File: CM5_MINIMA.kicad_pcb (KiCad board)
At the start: 4 copper layers, 54.6 x 57.1 mm, 97 parts, among them J101 USB_C_Receptacle_USB2.0, J501 690-019-298-412, J502 I2C, J601 JST_SHBM04B-SRSS-TB, Q501 DTC043ZEBTL, SW501 SW_Push, SW601 B3U-3000P, SW602 B3U-3000P, T401 7498111120AR, U401 TPD4EUSB30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

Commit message: production files added
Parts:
- added REF**: KiCad-Logo2_5mm_SilkScreen, Symbol:KiCad-Logo2_5mm_SilkScreen, F.Cu at (116.7, 77.8)

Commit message: JLCPCB
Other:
- board text added: "#808080FF"
- board text added: "0"
- board text added: "0 mm"
- board text added: "0.0000 mm / 0.0000 mm"
- board text added: "0.01 mm"
- board text added: "0.0152 mm"
- board text added: "0.02"
- board text added: "0.035 mm"
- board text added: "0.0994 mm"
- board text added: "0.3000 mm"
- board text added: "1"
- board text added: "1.265 mm"
- board text added: "1.5842 mm"
- board text added: "3.3"
- board text added: "4"
- board text added: "4.5"
- board text added: "54.5516 mm x 57.1400 mm"
- board text added: "B.Cu"
- board text added: "B.Mask"
- board text added: "B.Paste"
- board text added: "B.Silkscreen"
- board text added: "BOARD CHARACTERISTICS"
- board text added: "Board Thickness:"
- board text added: "Board overall dimensions:"
- board text added: "Bottom Silk Screen"
- board text added: "Bottom Solder Mask"
- board text added: "Bottom Solder Paste"
- board text added: "Castellated pads:"
- board text added: "Color"
- board text added: "Copper Finish:"
- board text added: "Copper Layer Count:"
- board text added: "Dielectric 1"
- board text added: "Dielectric 2"
- board text added: "Dielectric 3"
- board text added: "ENIG"
- board text added: "Edge card connectors:"
- board text added: "Epsilon R"
- board text added: "F.Cu"
- board text added: "F.Mask"
- board text added: "F.Paste"
- board text added: "F.Silkscreen"
- board text added: "FR4"
- board text added: "Impedance Control:"
- board text added: "In1.Cu"
- board text added: "In2.Cu"
- board text added: "Layer Name"
- board text added: "Loss Tangent"
- board text added: "Material"
- board text added: "Min hole diameter:"
- board text added: "Min track/spacing:"
- board text added: "No"
- board text added: "Not specified"
- board text added: "Plated Board Edge:"
- board text added: "Thickness (mm)"
- board text added: "Top Silk Screen"
- board text added: "Top Solder Mask"
- board text added: "Top Solder Paste"
- board text added: "Type"
- board text added: "Yes"
- board text added: "copper"
- board text added: "core"
- board text added: "prepreg"

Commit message: init
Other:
- board text removed: "#808080FF"
- board text removed: "0"
- board text removed: "0 mm"
- board text removed: "0.0000 mm / 0.0000 mm"
- board text removed: "0.01 mm"
- board text removed: "0.0152 mm"
- board text removed: "0.02"
- board text removed: "0.035 mm"
- board text removed: "0.0994 mm"
- board text removed: "0.3000 mm"
- board text removed: "1"
- board text removed: "1.265 mm"
- board text removed: "1.5842 mm"
- board text removed: "3.3"
- board text removed: "4"
- board text removed: "4.5"
- board text removed: "54.5516 mm x 57.1400 mm"
- board text removed: "B.Cu"
- board text removed: "B.Mask"
- board text removed: "B.Paste"
- board text removed: "B.Silkscreen"
- board text removed: "BOARD CHARACTERISTICS"
- board text removed: "Board Thickness:"
- board text removed: "Board overall dimensions:"
- board text removed: "Bottom Silk Screen"
- board text removed: "Bottom Solder Mask"
- board text removed: "Bottom Solder Paste"
- board text removed: "Castellated pads:"
- board text removed: "Color"
- board text removed: "Copper Finish:"
- board text removed: "Copper Layer Count:"
- board text removed: "Dielectric 1"
- board text removed: "Dielectric 2"
- board text removed: "Dielectric 3"
- board text removed: "ENIG"
- board text removed: "Edge card connectors:"
- board text removed: "Epsilon R"
- board text removed: "F.Cu"
- board text removed: "F.Mask"
- board text removed: "F.Paste"
- board text removed: "F.Silkscreen"
- board text removed: "FR4"
- board text removed: "Impedance Control:"
- board text removed: "In1.Cu"
- board text removed: "In2.Cu"
- board text removed: "Layer Name"
- board text removed: "Loss Tangent"
- board text removed: "Material"
- board text removed: "Min hole diameter:"
- board text removed: "Min track/spacing:"
- board text removed: "No"
- board text removed: "Not specified"
- board text removed: "Plated Board Edge:"
- board text removed: "Thickness (mm)"
- board text removed: "Top Silk Screen"
- board text removed: "Top Solder Mask"
- board text removed: "Top Solder Paste"
- board text removed: "Type"
- board text removed: "Yes"
- board text removed: "copper"
- board text removed: "core"
- board text removed: "prepreg"

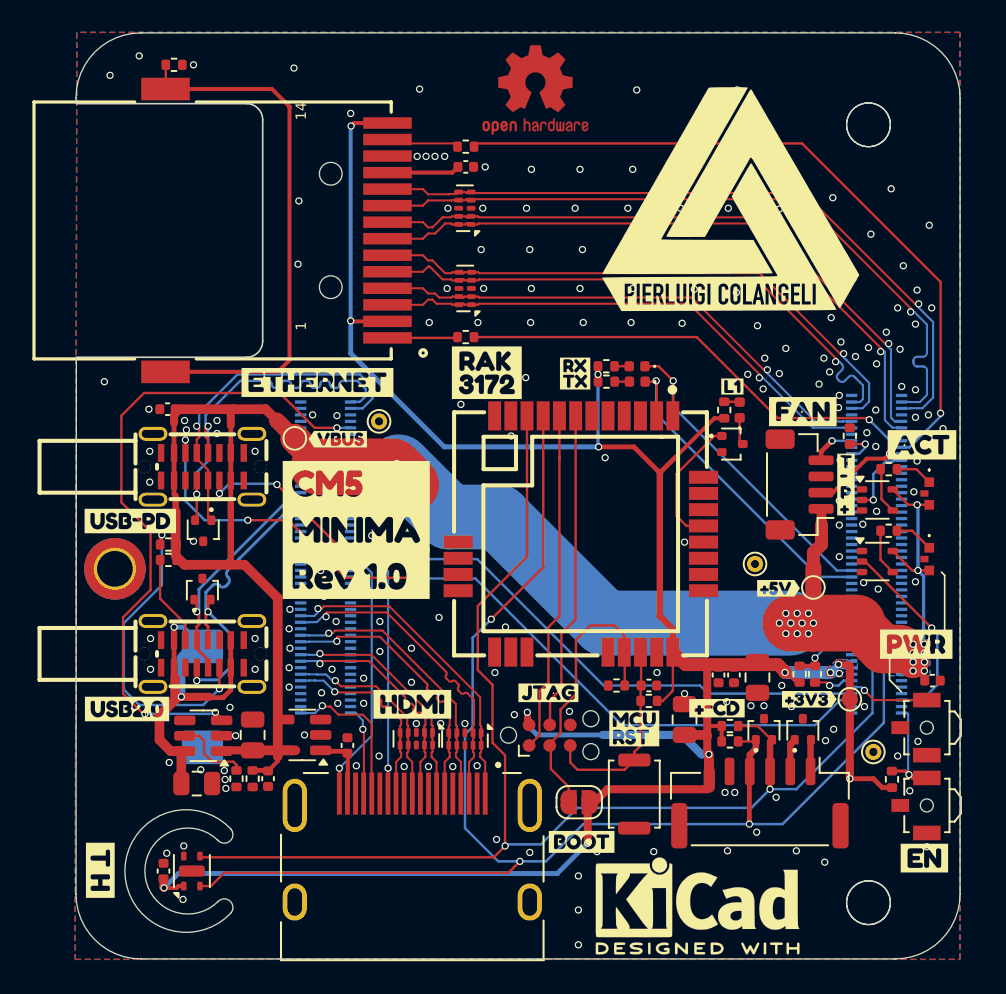
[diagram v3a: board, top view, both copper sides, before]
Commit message: diff pairs redesigned for pcbway capabilities
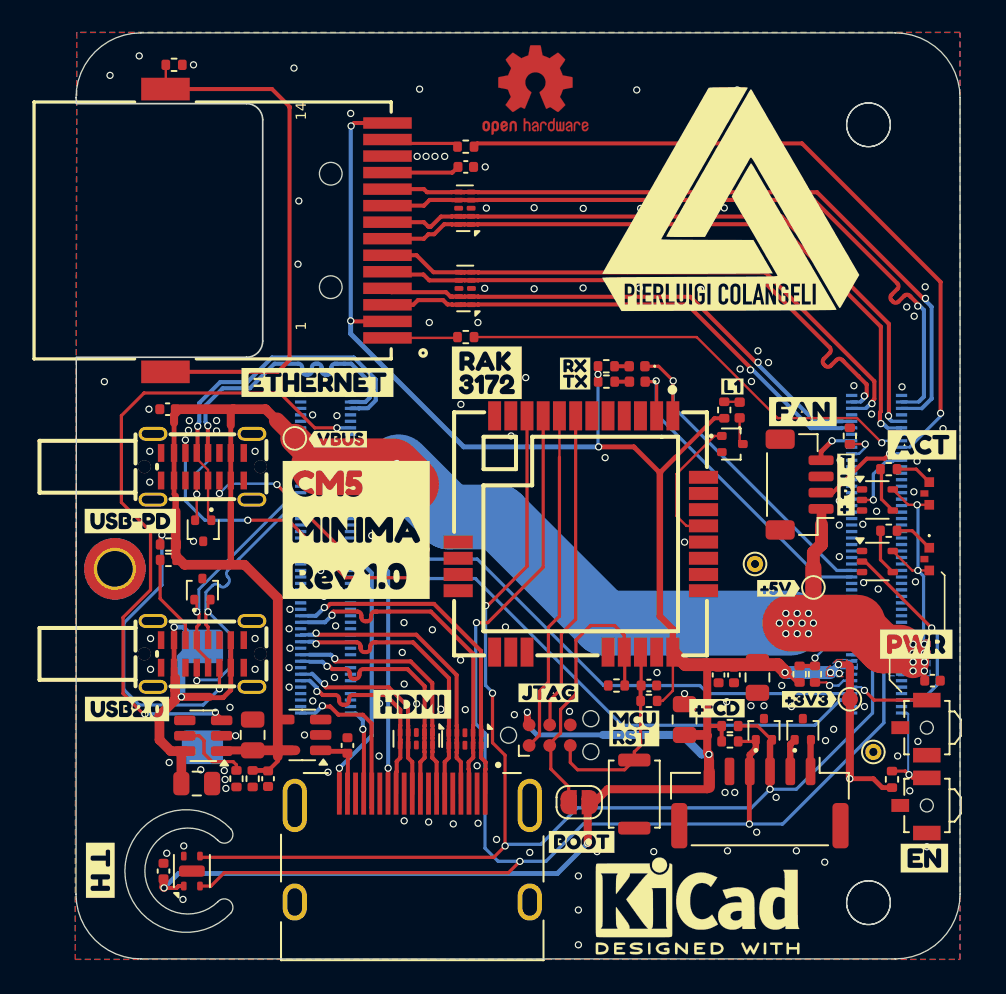
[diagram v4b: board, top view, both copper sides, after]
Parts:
- removed TP104: GND, TestPoint:TestPoint_THTPad_D1.0mm_Drill0.5mm
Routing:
- net /USB_C.D_P: track 21.5 -> 23.3 mm
- net /CM5/HDMI_PI.HDMI0_D2_N: track 19.9 -> 21.6 mm
- net /CM5/HDMI_PI.HDMI0_D2_P: track 20.0 -> 21.6 mm
- net /CM5/HDMI_PI.HDMI0_D0_P: track 14.8 -> 15.9 mm
- net /CM5/HDMI_PI.HDMI0_D0_N: track 14.8 -> 15.8 mm
- net /CM5/HDMI_PI.HDMI0_CK_N: track 12.4 -> 13.4 mm
- net /CM5/HDMI_PI.HDMI0_D1_P: track 17.3 -> 18.2 mm
- net /CM5/HDMI_PI.HDMI0_D1_N: track 17.3 -> 18.2 mm
- net /CM5/ETH_PI.TRD2_P: track 40.1 -> 40.9 mm
- net +3V3: track 153.7 -> 153.0 mm
- net /CM5/ETH_PI.TRD2_N: track 40.1 -> 40.8 mm
- net /CM5/ETH_PI.TRD3_P: track 44.0 -> 44.6 mm
- net /SDA: track 83.7 -> 83.4 mm, vias 2 -> 4
- net GND: vias 198 -> 137
- net (no net): vias 0 -> 12

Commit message: DRC ok
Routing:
- net GND: vias 137 -> 127
- net (no net): vias 12 -> 6

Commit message: impedance PCBway
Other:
- board text added: "0"
- board text added: "0 mm"
- board text added: "0.0000 mm / 0.0000 mm"
- board text added: "0.01 mm"
- board text added: "0.035 mm"
- board text added: "0.0525 mm"
- board text added: "0.196 mm"
- board text added: "0.3000 mm"
- board text added: "0.93 mm"
- board text added: "1"
- board text added: "1.5170 mm"
- board text added: "3.3"
- board text added: "4"
- board text added: "4.6"
- board text added: "4.74"
- board text added: "54.5516 mm x 57.1400 mm"
- board text added: "7628 RC46%"
- board text added: "B.Cu"
- board text added: "B.Mask"
- board text added: "B.Paste"
- board text added: "B.Silkscreen"
- board text added: "BOARD CHARACTERISTICS"
- board text added: "Board Thickness:"
- board text added: "Board overall dimensions:"
- board text added: "Bottom Silk Screen"
- board text added: "Bottom Solder Mask"
- board text added: "Bottom Solder Paste"
- board text added: "Castellated pads:"
- board text added: "Color"
- board text added: "Copper Finish:"
- board text added: "Copper Layer Count:"
- board text added: "Core"
- board text added: "Dielectric 1"
- board text added: "Dielectric 2"
- board text added: "Dielectric 3"
- board text added: "ENIG"
- board text added: "Edge card connectors:"
- board text added: "Epsilon R"
- board text added: "F.Cu"
- board text added: "F.Mask"
- board text added: "F.Paste"
- board text added: "F.Silkscreen"
- board text added: "FR4 natural"
- board text added: "Impedance Control:"
- board text added: "In1.Cu"
- board text added: "In2.Cu"
- board text added: "Layer Name"
- board text added: "Loss Tangent"
- board text added: "Material"
- board text added: "Min hole diameter:"
- board text added: "Min track/spacing:"
- board text added: "No"
- board text added: "Not specified"
- board text added: "Plated Board Edge:"
- board text added: "Thickness (mm)"
- board text added: "Top Silk Screen"
- board text added: "Top Solder Mask"
- board text added: "Top Solder Paste"
- board text added: "Type"
- board text added: "Yes"
- board text added: "copper"
- board text added: "core"
- board text added: "prepreg"

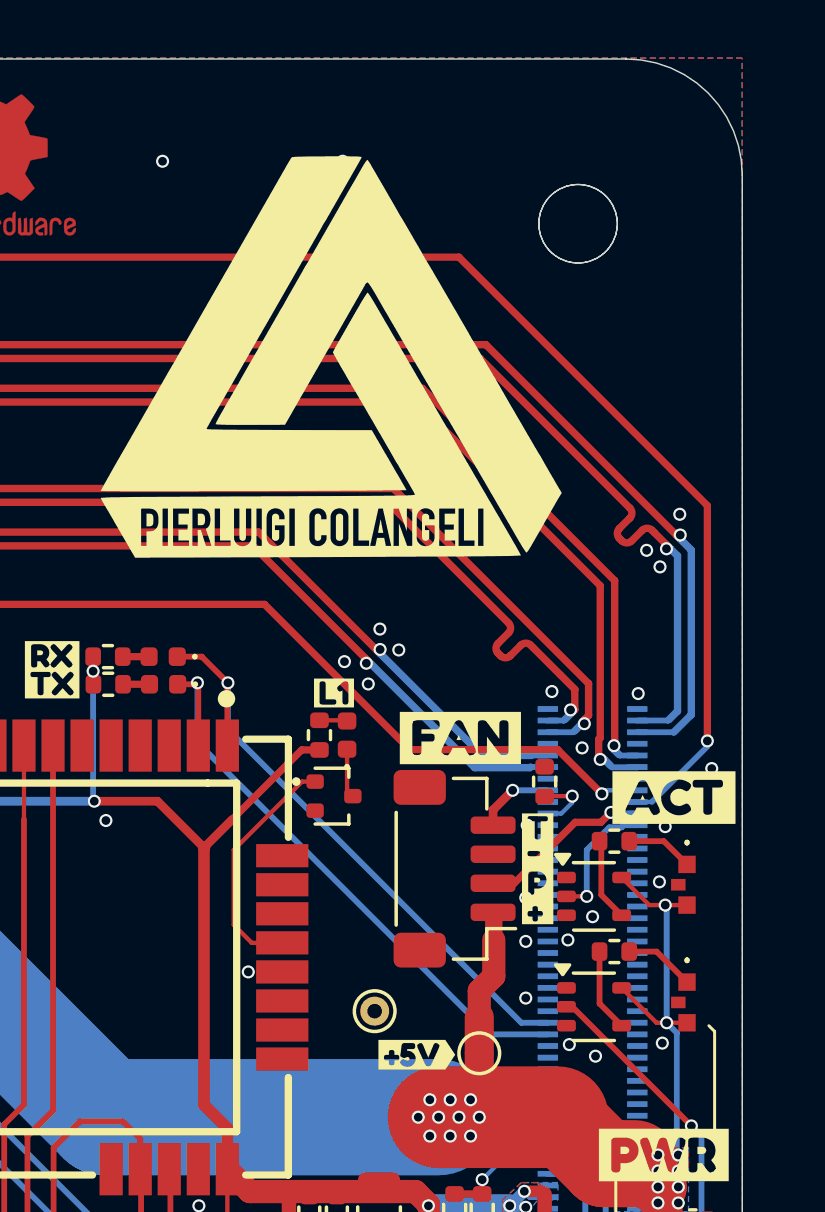
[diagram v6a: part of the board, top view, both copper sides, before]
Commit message: RAK to UART2 PCB
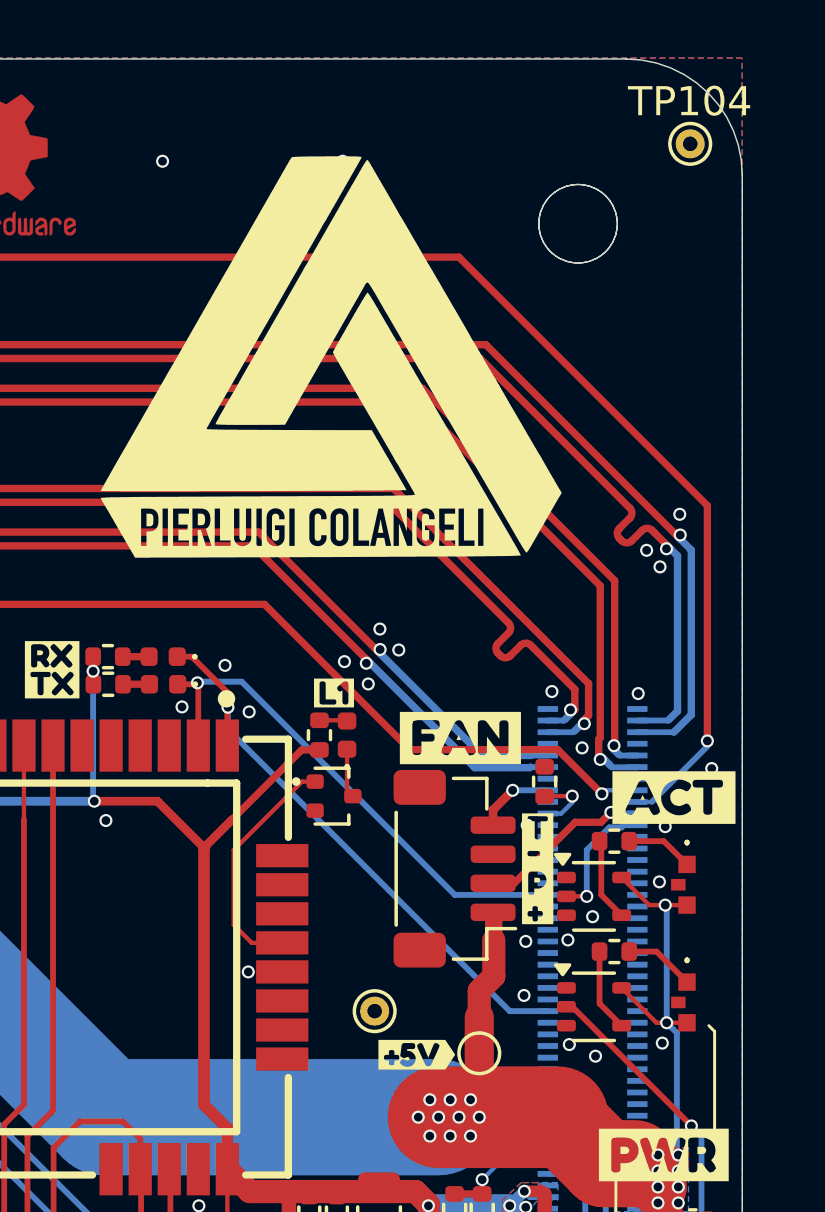
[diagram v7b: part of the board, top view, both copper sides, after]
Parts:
- added TP104: GND, TestPoint:TestPoint_THTPad_D1.0mm_Drill0.5mm, F.Cu at (131.1, 26.9)
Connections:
- Module301 pad 34: /CM5/GPIO5 -> /LoRaWAN/UART2_TX
- Module301 pad 54: /CM5/GPIO4 -> /LoRaWAN/UART2_RX
- Module301 pad 56: /LoRaWAN/UART2_RX -> /CM5/GPIO3
- Module301 pad 58: /LoRaWAN/UART2_TX -> /CM5/GPIO2
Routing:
- net /LoRaWAN/UART2_TX: track 21.1 -> 17.9 mm
- net /LoRaWAN/UART2_RX: track 21.1 -> 19.9 mm
- net GND: vias 127 -> 129
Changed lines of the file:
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@@
 	(net 48 "/CM5/GPIO19")
 	(net 49 "/CM5/GPIO22")
-	(net 50 "/CM5/GPIO4")
+	(net 50 "/CM5/GPIO2")
 	(net 51 "/CM5/GPIO23")
 	(net 52 "/CM5/GPIO15")
@@
 	(net 54 "/CM5/GPIO11")
 	(net 55 "/SDA")
-	(net 56 "/CM5/GPIO5")
+	(net 56 "/CM5/GPIO3")
 	(net 57 "/CM5/HDMI1_D2_N")
 	(net 58 "/CM5/PCIE_nRST")
@@
 		)
 	)
+	(footprint "TestPoint:TestPoint_THTPad_D1.0mm_Drill0.5mm"
+		(layer "F.Cu")
+		(at 131.11 26.85)
+		(descr "THT pad as test Point, diameter 1.0mm, hole diameter 0.5mm")
+		(tags "test point THT pad")
+		(property "Reference" "TP104"
+			(at 0 -1.448 0)
+			(layer "F.SilkS")
+			(effects
+				(font
+					(size 1 1)
+					(thickness 0.15)
+				)
+			)
+		)
+		(property "Value" "GND"
+			(at 0 1.55 0)
+			(layer "F.Fab")
+			(effects
+				(font
+					(size 1 1)
+					(thickness 0.15)
+				)
+			)
+		)
+		(property "Footprint" "TestPoint:TestPoint_THTPad_D1.0mm_Drill0.5mm"
+			(at 0 0 0)
+			(unlocked yes)
+			(layer "F.Fab")
+			(hide yes)
+			(effects
+				(font
+					(size 1.27 1.27)
+					(thickness 0.15)
+				)
+			)
+		)
+		(property "Datasheet" ""
+			(at 0 0 0)
+			(unlocked yes)
+			(layer "F.Fab")
+			(hide yes)
+			(effects
+				(font
+					(size 1.27 1.27)
+					(thickness 0.15)
+				)
+			)
+		)
+		(property "Description" "test point"
+			(at 0 0 0)
+			(unlocked yes)
+			(layer "F.Fab")
+			(hide yes)
+			(effects
+				(font
+					(size 1.27 1.27)
+					(thickness 0.15)
+				)
+			)
+		)
+		(property ki_fp_filters "Pin* Test*")
+		(sheetname "Root")
+		(sheetfile "CM5_MINIMA.kicad_sch")
+		(attr exclude_from_pos_files)
+		(fp_circle
+			(center 0 0)
+			(end 0 0.7)
+			(stroke
+				(width 0.12)
+				(type solid)
+			)
+			(fill none)
+			(layer "F.SilkS")
+		)
+		(fp_circle
+			(center 0 0)
+			(end 1 0)
+			(stroke
+				(width 0.05)
+				(type solid)
+			)
+			(fill none)
+			(layer "F.CrtYd")
+		)
+		(fp_text user "${REFERENCE}"
+			(at 0 -1.45 0)
+			(layer "F.Fab")
+			(effects
+				(font
+					(size 1 1)
+					(thickness 0.15)
+				)
+			)
+		)
+		(pad "1" thru_hole circle
+			(at 0 0)
+			(size 1 1)
+			(drill 0.5)
+			(layers "*.Cu" "*.Mask")
+			(remove_unused_layers no)
+			(net 1 "GND")
+			(pinfunction "1")
+			(pintype "passive")
+		)
+	)
 	(footprint "Resistor_SMD:R_0402_1005Metric"
 		(layer "F.Cu")
@@
 			(size 0.2 0.7)
 			(layers "B.Cu" "B.Paste" "B.Mask")
-			(net 56 "/CM5/GPIO5")
+			(net 177 "/LoRaWAN/UART2_TX")
 			(pinfunction "GPIO5")
 			(pintype "passive")
@@
 			(size 0.2 0.7)
 			(layers "B.Cu" "B.Paste" "B.Mask")
-			(net 50 "/CM5/GPIO4")
+			(net 176 "/LoRaWAN/UART2_RX")
 			(pinfunction "GPIO4")
-			(pintype "passive+no_connect")
+			(pintype "passive")
 		)
 		(pad "55" smd rect
@@
 			(size 0.2 0.7)
 			(layers "B.Cu" "B.Paste" "B.Mask")
-			(net 176 "/LoRaWAN/UART2_RX")
+			(net 56 "/CM5/GPIO3")
 			(pinfunction "GPIO3")
-			(pintype "passive")
+			(pintype "passive+no_connect")
 		)
 		(pad "57" smd rect
@@
 			(size 0.2 0.7)
 			(layers "B.Cu" "B.Paste" "B.Mask")
-			(net 177 "/LoRaWAN/UART2_TX")
+			(net 50 "/CM5/GPIO2")
 			(pinfunction "GPIO2")
-			(pintype "passive")
+			(pintype "passive+no_connect")
 		)
 		(pad "59" smd rect
@@
 	)
 	(via
+		(at 115.1 44.8)
+		(size 0.45)
+		(drill 0.3)
+		(layers "F.Cu" "B.Cu")
+		(free yes)
+		(net 1)
+	)
+	(via
 		(at 88.2 67.3)
 		(size 0.45)
@@
 	)
 	(via
+		(at 113.62 46.23)
+		(size 0.45)
+		(drill 0.3)
+		(layers "F.Cu" "B.Cu")
+		(free yes)
+		(net 1)
+	)
+	(via
 		(at 94.45 47.55)
 		(size 0.45)
@@
 	)
 	(via
+		(at 115.93 46.4)
+		(size 0.45)
+		(drill 0.3)
+		(layers "F.Cu" "B.Cu")
+		(free yes)
+		(net 1)
+	)
+	(via
 		(at 102.08 62.63)
 		(size 0.45)
@@
 	)
 	(via
-		(at 125.45 52.8)
-		(size 0.45)
-		(drill 0.3)
-		(layers "F.Cu" "B.Cu")
-		(free yes)
-		(net 1)
-	)
-	(via
 		(at 82.9 51.65)
 		(size 0.45)
@@
 	)
 	(via
-		(at 125.45 56.25)
+		(at 125.39 56.16)
 		(size 0.45)
 		(drill 0.3)
@@
 	)
 	(segment
-		(start 114.3 44.5)
-		(end 115.2 45.4)
+		(start 115.2 46.24)
+		(end 115.18 46.26)
+		(width 0.2)
+		(layer "F.Cu")
+		(net 176)
+	)
+	(segment
+		(start 115.18 46.26)
+		(end 115.18 47.56)
+		(width 0.2)
+		(layer "F.Cu")
+		(net 176)
+	)
+	(segment
+		(start 115.2 46.24)
+		(end 115.2 45.742893)
 		(width 0.2)
 		(layer "F.Cu")
@@
 	)
 	(segment
-		(start 113.455 44.5)
-		(end 114.3 44.5)
+		(start 113.957107 44.5)
+		(end 113.455 44.5)
 		(width 0.2)
 		(layer "F.Cu")
@@
 	)
 	(segment
-		(start 115.18 47.56)
-		(end 115.18 45.42)
+		(start 115.2 45.742893)
+		(end 113.957107 44.5)
 		(width 0.2)
 		(layer "F.Cu")
@@
 	)
 	(via
-		(at 115.2 45.4)
+		(at 115.2 46.24)
 		(size 0.45)
 		(drill 0.3)
@@
 	)
 	(segment
-		(start 115.2 45.4)
-		(end 115.2 47)
+		(start 124.9 56.7)
+		(end 126.21 56.7)
 		(width 0.2)
 		(layer "B.Cu")
@@
 	)
 	(segment
-		(start 115.2 47)
-		(end 125.3 57.1)
+		(start 115.2 46.24)
+		(end 115.2 47)
 		(width 0.2)
 		(layer "B.Cu")
@@
 	)
 	(segment
-		(start 125.3 57.1)
-		(end 126.21 57.1)
+		(start 115.2 47)
+		(end 124.9 56.7)
 		(width 0.2)
 		(layer "B.Cu")
@@
 	)
 	(segment
-		(start 124.2 57.5)
-		(end 126.21 57.5)
+		(start 123.01 52.7)
+		(end 126.21 52.7)
+		(width 0.2)
+		(layer "B.Cu")
+		(net 177)
+	)
+	(segment
+		(start 114.19 45.36)
+		(end 115.67 45.36)
 		(width 0.2)
 		(layer "B.Cu")
@@
 	(segment
 		(start 114.15 45.4)
-		(end 114.15 47.45)
+		(end 114.19 45.36)
 		(width 0.2)
 		(layer "B.Cu")
@@
 	)
 	(segment
-		(start 114.15 47.45)
-		(end 124.2 57.5)
+		(start 115.67 45.36)
+		(end 123.01 52.7)
 		(width 0.2)
 		(layer "B.Cu")
